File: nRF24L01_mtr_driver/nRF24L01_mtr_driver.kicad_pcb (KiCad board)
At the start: 4 copper layers, 60.1 x 39.9 mm, 147 parts, among them J1 Micro USB, J2 I/O, J4 VBAT, J5 MTR, J6 SERVO, J7 ICSP, Q1 AO4484, Q2 AO4484, Q3 AO4484, Q4 AO4484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

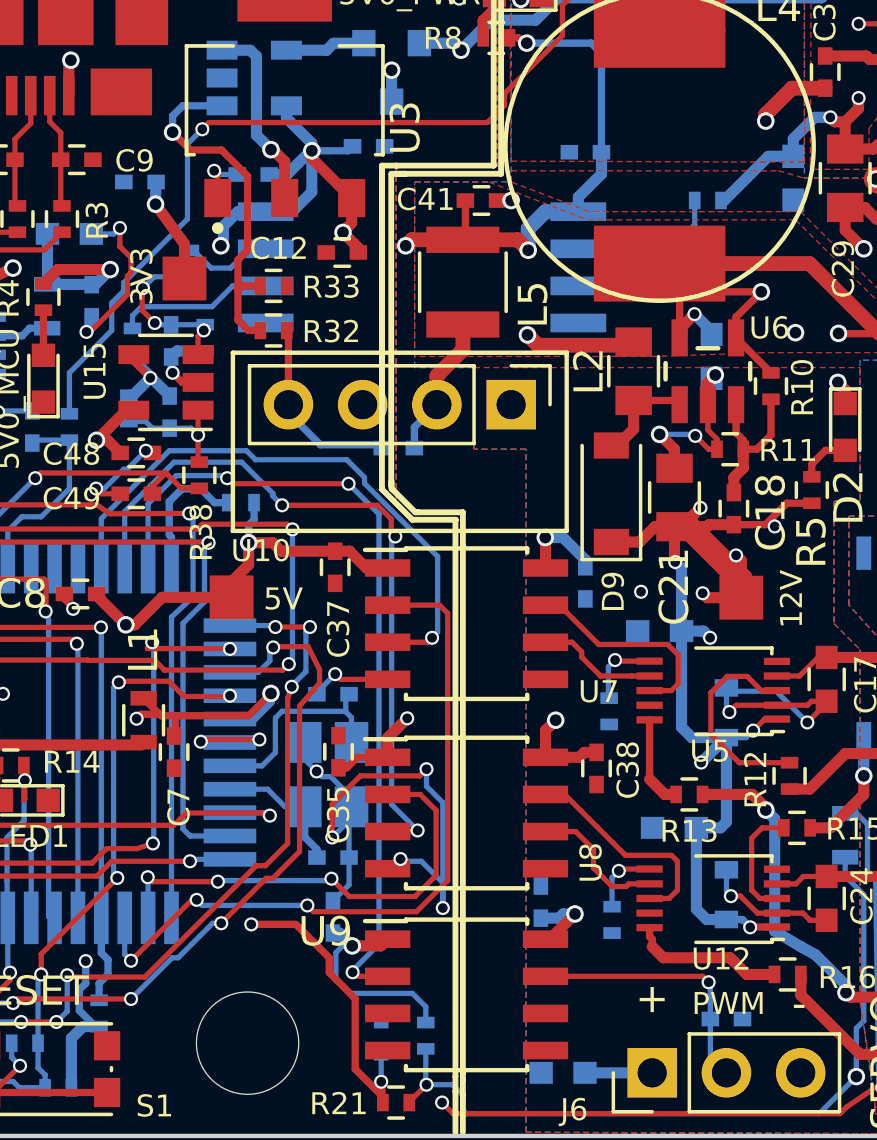
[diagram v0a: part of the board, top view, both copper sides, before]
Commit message: fixed ROI-0505S footprint and added its 3 model
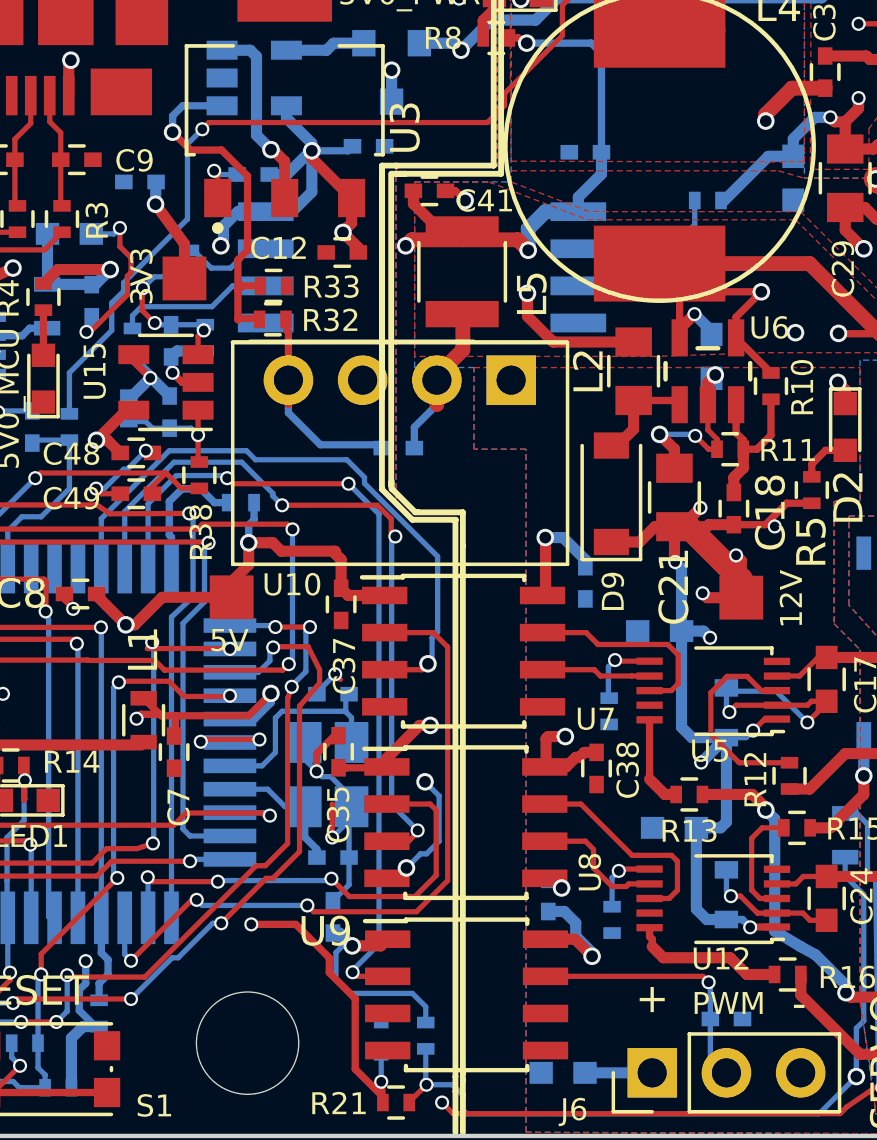
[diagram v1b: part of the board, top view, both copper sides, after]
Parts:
- moved C41 1.81 mm to (87.0, 52.5)
- moved C37 1.29 mm to (84.0, 66.6)
- moved U7 0.95 mm to (88.2, 68.2)
- moved U10 0.84 mm to (89.8, 59.0)
- moved R32 0.38 mm to (81.6, 56.9)
- moved L5 0.36 mm to (88.1, 55.3)
- moved C39 0.34 mm to (91.1, 76.6)
- moved U8 0.33 mm to (88.2, 74.1)
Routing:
- net 5V0_MCU: track 174.1 -> 188.5 mm
- net GNDA: track 139.8 -> 132.4 mm, vias 37 -> 36
- net 5V0_PWR: track 98.9 -> 104.1 mm
- net 12V_PWR: track 41.7 -> 39.6 mm, vias 10 -> 9
- net GND_PWR: track 26.1 -> 27.8 mm, vias 12 -> 13
- net /IN1_MCU: track 25.2 -> 24.2 mm
- net /EN1_MCU: track 20.2 -> 21.1 mm

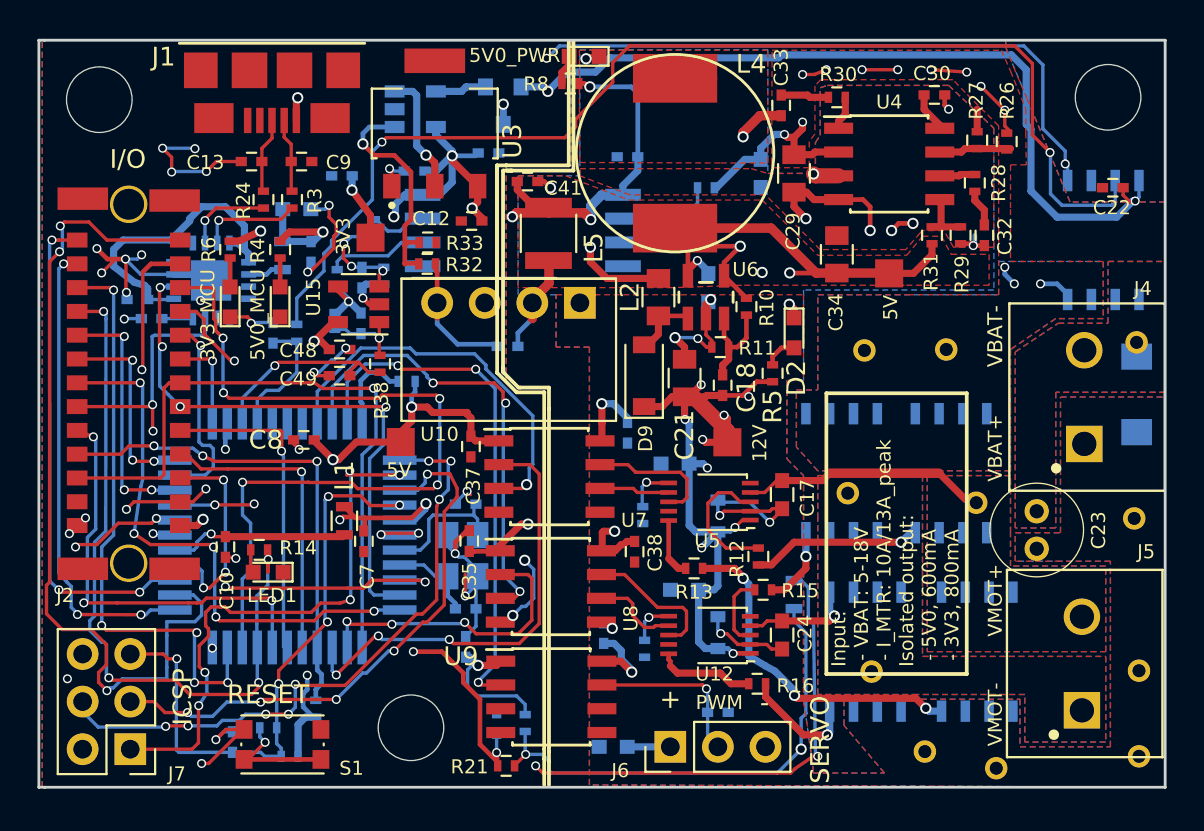
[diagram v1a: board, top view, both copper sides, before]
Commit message: fixed U14 position
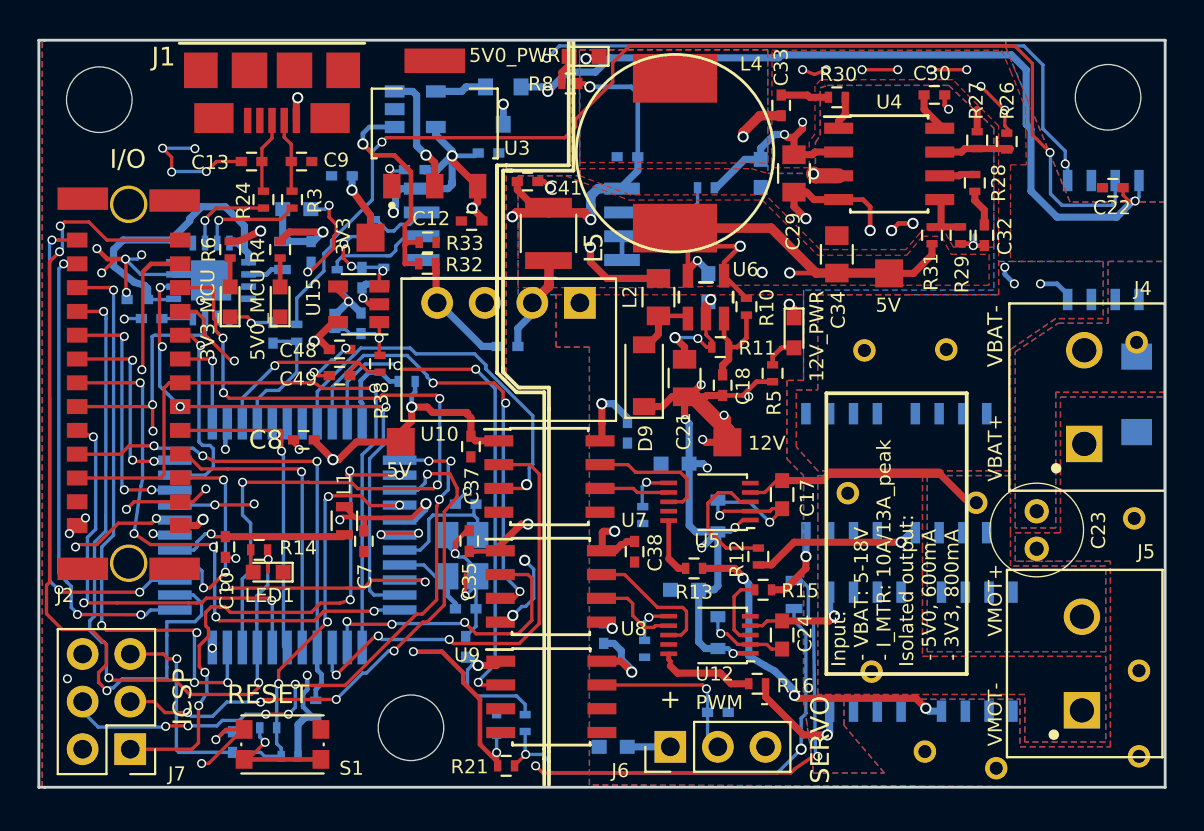
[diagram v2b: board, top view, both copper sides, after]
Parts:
- moved U14 0.33 mm to (86.7, 54.8)
- moved C45 0.08 mm to (81.0, 51.9)
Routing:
- net GND_PWR: track 27.8 -> 29.1 mm
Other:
- board text added: "12V_PWR"
